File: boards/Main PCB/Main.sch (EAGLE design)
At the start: 114 parts, among them CN1 MINIB, CN2 MINIB, IC1 FT232RL, IC2 FT232RL, IC4 OKR-T_3-W12-C, J1 3_PIN_JST-XH, J2 2_PIN_JST-XH, J3 5_PIN_JST-XH, Q4 BSS138, Q5 BSS138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

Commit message: Finished moving encoders and reset pin
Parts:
- removed C33: 10nF, rcl:C-USC0805
- added JP1: (no value), pinhead:PINHD-1X1
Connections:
- net GND: no longer C33.2
- net NRST: no longer C33.1
- net RESET: now also JP1.1
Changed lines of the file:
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@@
 <part name="R37" library="resistor" library_urn="urn:adsk.eagle:library:348" deviceset="R-US_" device="R0805" package3d_urn="urn:adsk.eagle:package:26059/1" value="100"/>
 <part name="JP2" library="pinhead" library_urn="urn:adsk.eagle:library:325" deviceset="PINHD-1X5" device="" package3d_urn="urn:adsk.eagle:package:22469/2"/>
-<part name="C33" library="rcl" library_urn="urn:adsk.eagle:library:334" deviceset="C-US" device="C0805" package3d_urn="urn:adsk.eagle:package:23617/2" value="10nF">
-<spice>
-<pinmapping spiceprefix="C">
-<pinmap gate="G$1" pin="1" pinorder="1"/>
-<pinmap gate="G$1" pin="2" pinorder="2"/>
-</pinmapping>
-</spice>
-<attribute name="SPICEPREFIX" value="10nF"/>
-</part>
-<part name="GND48" library="supply1" library_urn="urn:adsk.eagle:library:371" deviceset="GND" device=""/>
+<part name="JP1" library="pinhead" library_urn="urn:adsk.eagle:library:325" deviceset="PINHD-1X1" device="" package3d_urn="urn:adsk.eagle:package:22485/2"/>
 </parts>
 <sheets>
@@
 <text x="68.58" y="154.94" size="1.778" layer="91">IMU</text>
 <text x="226.06" y="152.4" size="1.778" layer="91">Lidar UART Converter</text>
-<text x="203.2" y="342.9" size="1.778" layer="91">Reset Circuitry</text>
+<text x="203.2" y="327.66" size="1.778" layer="91">Reset Circuitry</text>
 <text x="424.18" y="228.6" size="1.778" layer="91">External Crystal</text>
 <text x="480.06" y="289.56" size="1.778" layer="91">3.3V-5V Logic Converter For Display</text>
@@
 </instance>
 <instance part="R37" gate="G$1" x="220.98" y="314.96" smashed="yes" rot="R90">
-<attribute name="NAME" x="219.4814" y="311.15" size="1.778" layer="95" rot="R90"/>
 <attribute name="VALUE" x="224.282" y="311.15" size="1.778" layer="96" rot="R90"/>
 </instance>
@@
 <attribute name="VALUE" x="209.55" y="238.76" size="1.778" layer="96" rot="R180"/>
 </instance>
-<instance part="C33" gate="G$1" x="218.44" y="297.18" smashed="yes" rot="R270">
-<attribute name="VALUE" x="214.249" y="296.164" size="1.778" layer="96" rot="R270"/>
-</instance>
-<instance part="GND48" gate="1" x="210.82" y="294.64" smashed="yes">
-<attribute name="VALUE" x="208.28" y="292.1" size="1.778" layer="96"/>
+<instance part="JP1" gate="G$1" x="213.36" y="337.82" smashed="yes" rot="R90">
+<attribute name="NAME" x="210.185" y="331.47" size="1.778" layer="95" rot="R90"/>
+<attribute name="VALUE" x="218.44" y="331.47" size="1.778" layer="96" rot="R90"/>
 </instance>
 </instances>
@@
 <pinref part="RESET" gate="G$1" pin="3"/>
 <wire x1="213.36" y1="304.8" x2="215.9" y2="304.8" width="0.1524" layer="91"/>
-<wire x1="213.36" y1="304.8" x2="205.74" y2="304.8" width="0.1524" layer="91"/>
-<wire x1="205.74" y1="304.8" x2="205.74" y2="309.88" width="0.1524" layer="91"/>
 <pinref part="C13" gate="G$1" pin="2"/>
-<wire x1="195.58" y1="314.96" x2="195.58" y2="309.88" width="0.1524" layer="91"/>
-<wire x1="205.74" y1="309.88" x2="195.58" y2="309.88" width="0.1524" layer="91"/>
+<wire x1="195.58" y1="314.96" x2="195.58" y2="304.8" width="0.1524" layer="91"/>
+<wire x1="213.36" y1="304.8" x2="195.58" y2="304.8" width="0.1524" layer="91"/>
 <wire x1="213.36" y1="304.8" x2="210.82" y2="304.8" width="0.1524" layer="91"/>
 </segment>
@@
 <wire x1="452.12" y1="269.24" x2="457.2" y2="269.24" width="0.1524" layer="91"/>
 </segment>
-<segment>
-<pinref part="GND48" gate="1" pin="GND"/>
-<pinref part="C33" gate="G$1" pin="2"/>
-<wire x1="210.82" y1="297.18" x2="213.36" y2="297.18" width="0.1524" layer="91"/>
-</segment>
 </net>
 <net name="N$36" class="0">
@@
 <pinref part="RESET" gate="G$1" pin="1"/>
 <junction x="210.82" y="325.12"/>
-<wire x1="210.82" y1="325.12" x2="215.9" y2="325.12" width="0.1524" layer="91"/>
+<wire x1="210.82" y1="325.12" x2="213.36" y2="325.12" width="0.1524" layer="91"/>
+<wire x1="213.36" y1="325.12" x2="215.9" y2="325.12" width="0.1524" layer="91"/>
 <wire x1="220.98" y1="325.12" x2="215.9" y2="325.12" width="0.1524" layer="91"/>
 <junction x="215.9" y="325.12"/>
 <pinref part="R37" gate="G$1" pin="2"/>
 <wire x1="220.98" y1="325.12" x2="220.98" y2="320.04" width="0.1524" layer="91"/>
+<pinref part="JP1" gate="G$1" pin="1"/>
+<wire x1="213.36" y1="335.28" x2="213.36" y2="325.12" width="0.1524" layer="91"/>
+<junction x="213.36" y="325.12"/>
 </segment>
 </net>
@@
 <wire x1="220.98" y1="309.88" x2="220.98" y2="297.18" width="0.1524" layer="91"/>
 <label x="233.68" y="297.18" size="1.778" layer="95" rot="R180" xref="yes"/>
-<pinref part="C33" gate="G$1" pin="1"/>
-<junction x="220.98" y="297.18"/>
-</segment>
-<segment>
+</segment>
+<segment>

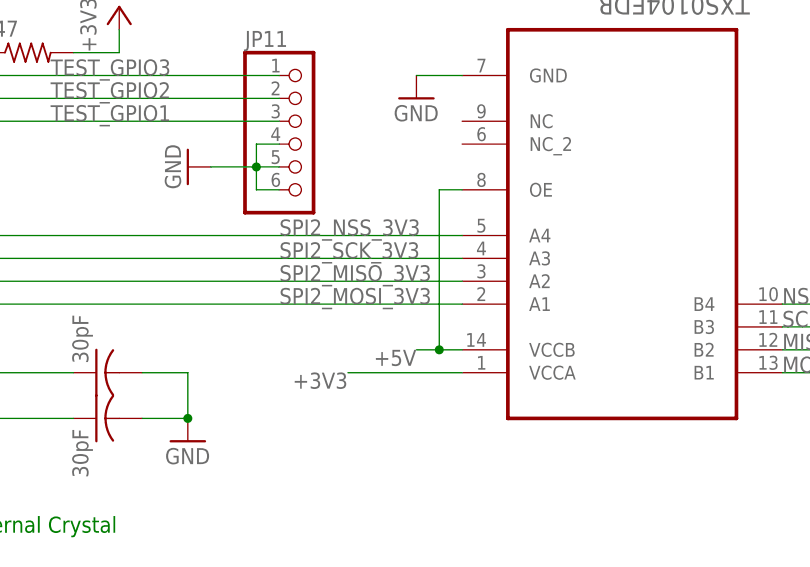
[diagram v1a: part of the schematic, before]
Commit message: Fixing logic converter circuit
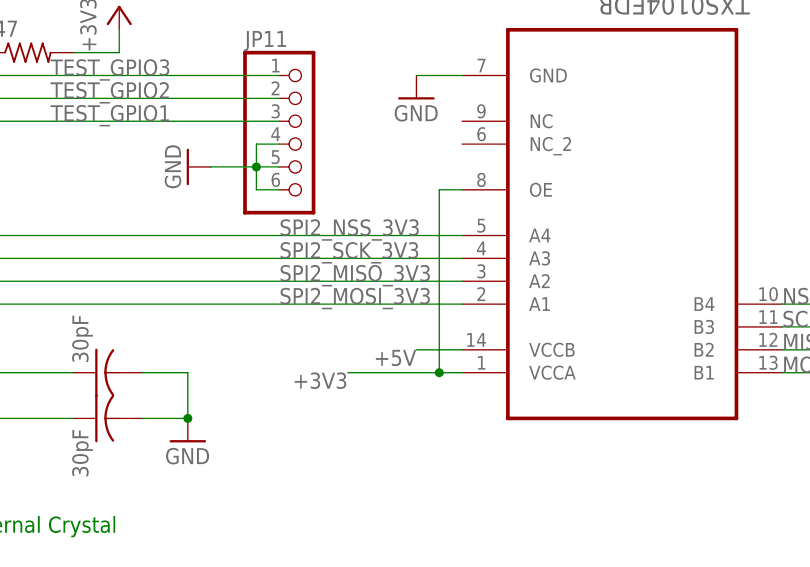
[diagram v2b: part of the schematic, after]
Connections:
- net +3V3: now also U4.OE
- net +5V: no longer U4.OE
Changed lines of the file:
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@@
 <?xml version="1.0" encoding="utf-8"?>
 <!DOCTYPE eagle SYSTEM "eagle.dtd">
-<eagle version="9.3.1">
+<eagle version="9.2.2">
 <drawing>
 <settings>
@@
 <segment>
 <pinref part="U4" gate="A" pin="VCCA"/>
-<wire x1="480.06" y1="246.38" x2="467.36" y2="246.38" width="0.1524" layer="91"/>
+<wire x1="480.06" y1="246.38" x2="477.52" y2="246.38" width="0.1524" layer="91"/>
 <label x="467.36" y="246.38" size="1.778" layer="95" rot="R180"/>
+<pinref part="U4" gate="A" pin="OE"/>
+<wire x1="477.52" y1="246.38" x2="467.36" y2="246.38" width="0.1524" layer="91"/>
+<wire x1="480.06" y1="266.7" x2="477.52" y2="266.7" width="0.1524" layer="91"/>
+<wire x1="477.52" y1="266.7" x2="477.52" y2="246.38" width="0.1524" layer="91"/>
+<junction x="477.52" y="246.38"/>
 </segment>
 <segment>
@@
 <segment>
 <pinref part="U4" gate="A" pin="VCCB"/>
-<wire x1="480.06" y1="248.92" x2="477.52" y2="248.92" width="0.1524" layer="91"/>
-<pinref part="U4" gate="A" pin="OE"/>
-<wire x1="477.52" y1="248.92" x2="474.98" y2="248.92" width="0.1524" layer="91"/>
-<wire x1="480.06" y1="266.7" x2="477.52" y2="266.7" width="0.1524" layer="91"/>
-<wire x1="477.52" y1="266.7" x2="477.52" y2="248.92" width="0.1524" layer="91"/>
-<junction x="477.52" y="248.92"/>
+<wire x1="480.06" y1="248.92" x2="474.98" y2="248.92" width="0.1524" layer="91"/>
 <label x="474.98" y="248.92" size="1.778" layer="95" rot="R180"/>
 </segment>

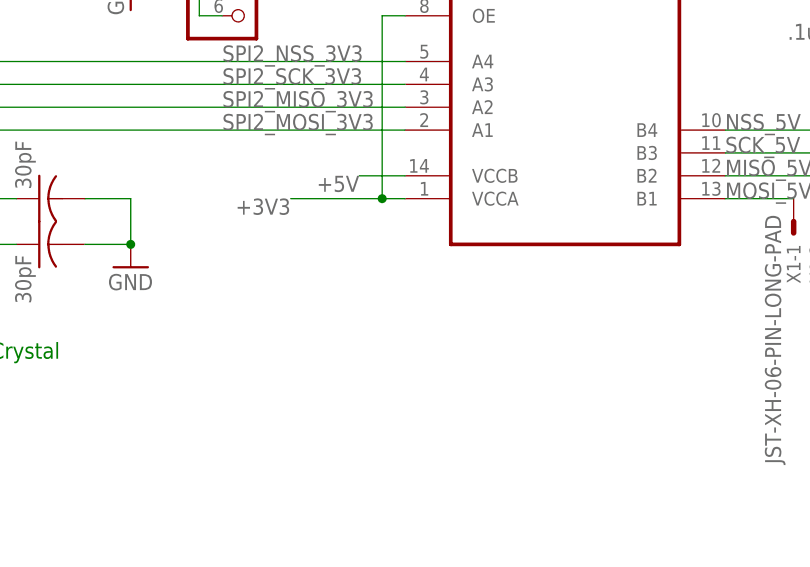
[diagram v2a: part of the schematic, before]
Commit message: Adding decoupling cap at 3V into logic converter
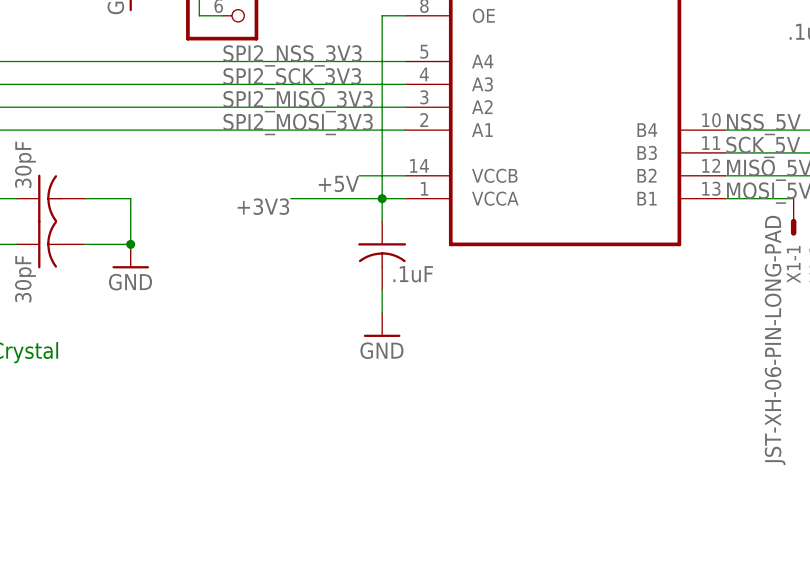
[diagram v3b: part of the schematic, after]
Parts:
- added C33: .1uF, rcl:C-USC0805
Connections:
- net +3V3: now also C33.1
- net GND: now also C33.2
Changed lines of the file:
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@@
 <part name="JP2" library="pinhead" library_urn="urn:adsk.eagle:library:325" deviceset="PINHD-1X5" device="" package3d_urn="urn:adsk.eagle:package:22469/2"/>
 <part name="JP1" library="pinhead" library_urn="urn:adsk.eagle:library:325" deviceset="PINHD-1X1" device="" package3d_urn="urn:adsk.eagle:package:22485/2"/>
+<part name="C33" library="rcl" library_urn="urn:adsk.eagle:library:334" deviceset="C-US" device="C0805" package3d_urn="urn:adsk.eagle:package:23617/2" value=".1uF"/>
+<part name="GND48" library="supply1" library_urn="urn:adsk.eagle:library:371" deviceset="GND" device=""/>
 </parts>
 <sheets>
@@
 <attribute name="NAME" x="210.185" y="331.47" size="1.778" layer="95" rot="R90"/>
 <attribute name="VALUE" x="218.44" y="331.47" size="1.778" layer="96" rot="R90"/>
+</instance>
+<instance part="C33" gate="G$1" x="477.52" y="241.3" smashed="yes">
+<attribute name="VALUE" x="478.536" y="237.109" size="1.778" layer="96"/>
+</instance>
+<instance part="GND48" gate="1" x="477.52" y="231.14" smashed="yes">
+<attribute name="VALUE" x="474.98" y="228.6" size="1.778" layer="96"/>
 </instance>
 </instances>
@@
 <wire x1="477.52" y1="266.7" x2="477.52" y2="246.38" width="0.1524" layer="91"/>
 <junction x="477.52" y="246.38"/>
+<pinref part="C33" gate="G$1" pin="1"/>
+<wire x1="477.52" y1="246.38" x2="477.52" y2="243.84" width="0.1524" layer="91"/>
 </segment>
 <segment>
@@
 <wire x1="452.12" y1="269.24" x2="457.2" y2="269.24" width="0.1524" layer="91"/>
 </segment>
+<segment>
+<pinref part="C33" gate="G$1" pin="2"/>
+<pinref part="GND48" gate="1" pin="GND"/>
+<wire x1="477.52" y1="236.22" x2="477.52" y2="233.68" width="0.1524" layer="91"/>
+</segment>
 </net>

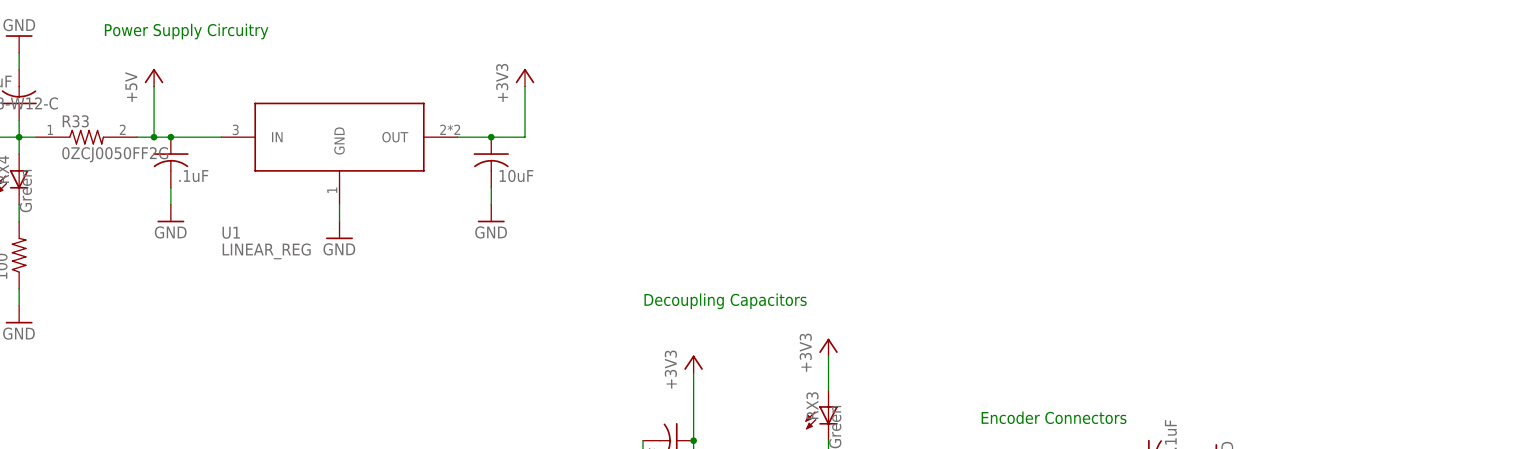
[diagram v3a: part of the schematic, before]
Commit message: Added a TL431 and Thyristor
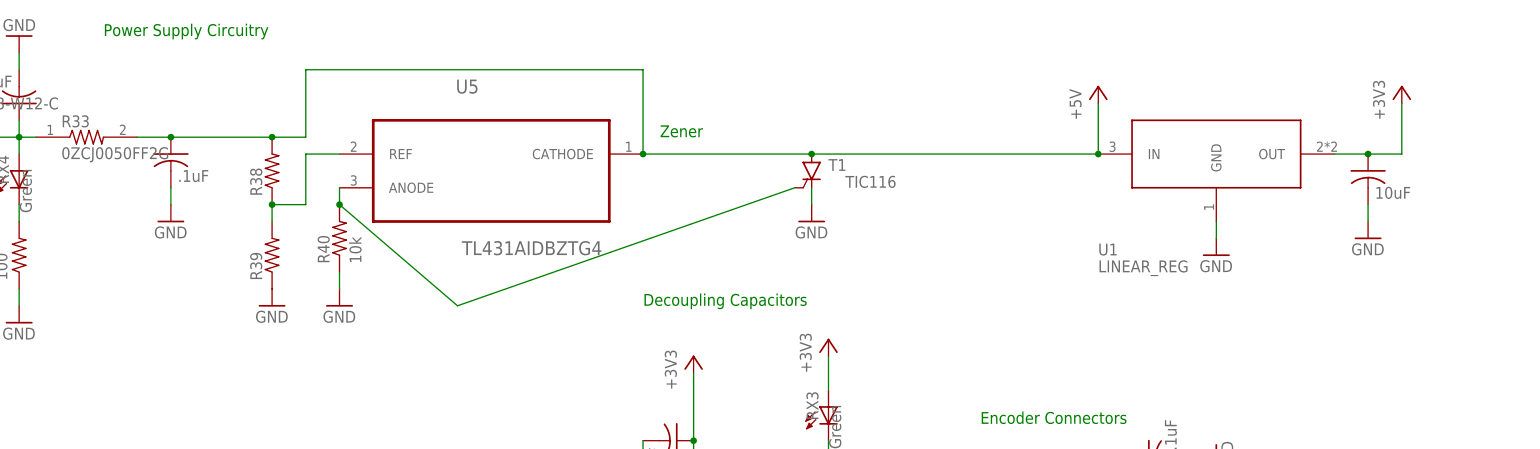
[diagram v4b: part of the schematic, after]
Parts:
- added R38, R39: (no value), resistor:R-US_R0805
- added R40: 10k, resistor:R-US_R0805
- added T1: TIC116, triac:TIC116
- added U5: TL431AIDBZTG4, main_library:TL431AIDBZTG4
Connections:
- new net N$25: R38.1, R39.2, U5.REF
- new net N$30: R40.2, T1.G, U5.ANODE
- net +5V: now also R38.2, T1.A, U5.CATHODE
- net GND: now also R39.1, R40.1, T1.C
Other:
- note added: "Zener"
- moved on the sheet: U1
